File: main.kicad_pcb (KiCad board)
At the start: 2 copper layers, 228.6 x 70.6 mm, 134 parts, among them J1 Conn_02x16_Row_Letter_First, J10 Conn_01x26_Pin, J11 Conn_ARM_JTAG_SWD_10, J2 Conn_01x05, J3 Conn_01x02, J4 Screw_Terminal_01x02, J5 Screw_Terminal_01x10, J6 Screw_Terminal_01x10, J7 Screw_Terminal_01x02, J8 Screw_Terminal_01x10, J9 Screw_Terminal_01x10, U10 TLP3558A, U11 TLP3558A, U12 TLP3558A, U13 TLP3558A, U14 TLP3558A, U15 TLP3558A, U16 TLP3558A, U17 TLP3558A, U18 TLP3558A, U19 TLP3558A, U2 NCP1117-3.3_TO252, U20 TLP3558A, U21 TLP3558A, U22 TLP3558A, U23 TLP3558A, U24 TLP3558A, U25 TLP3558A, U26 TLP3558A, U27 TLP3558A, U28 TLP3558A, U29 TLP3558A, U3 STM32G070KBT6, U30 TLP3558A, U31 TLP3558A, U32 TLP3558A, U33 TLP3558A, U34 TLP3558A, U35 TLP3558A, U36 TLP3558A, U37 TLP3558A, U38 TLP3558A, U39 TLP3558A, U4 TLP3558A, U40 TLP3558A, U41 TLP3558A, U42 TLP3558A, U43 TLP3558A, U44 TLP3558A, U45 TLP3558A, U46 TLP3558A, U47 TLP3558A, U5 TLP3558A, U6 TLP3558A, U7 TLP3558A, U8 TLP3558A, U9 TLP3558A

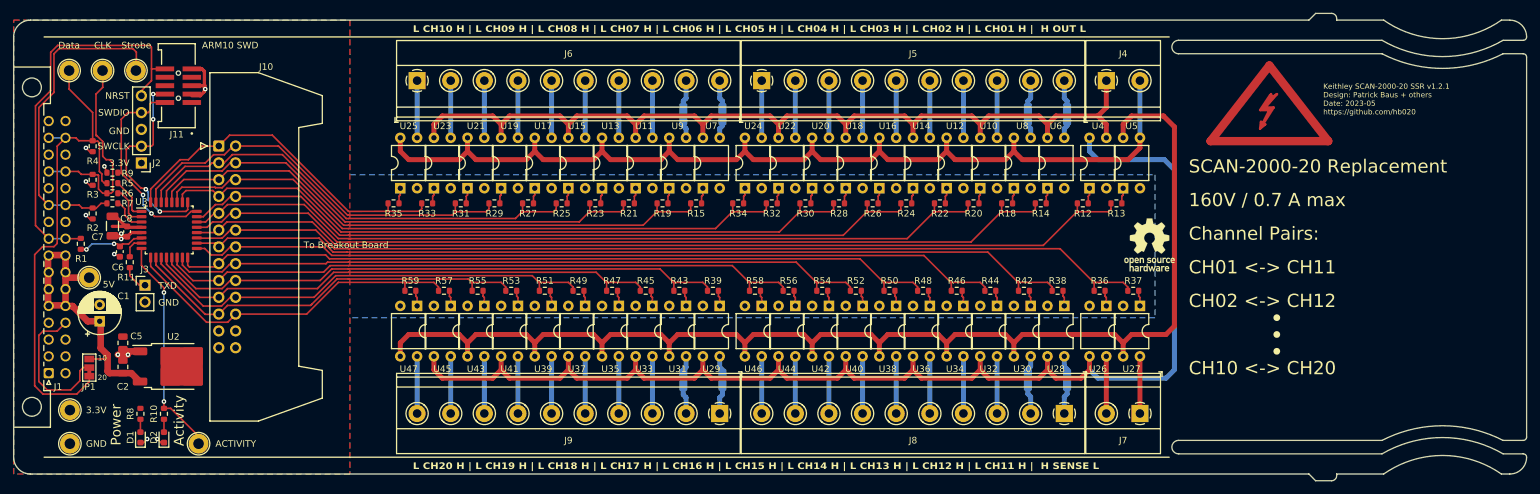
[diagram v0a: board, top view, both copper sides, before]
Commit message: Version 1.6
Created a high-voltage rated scan board.

Control is done completely in logic to avoid programming an MCU
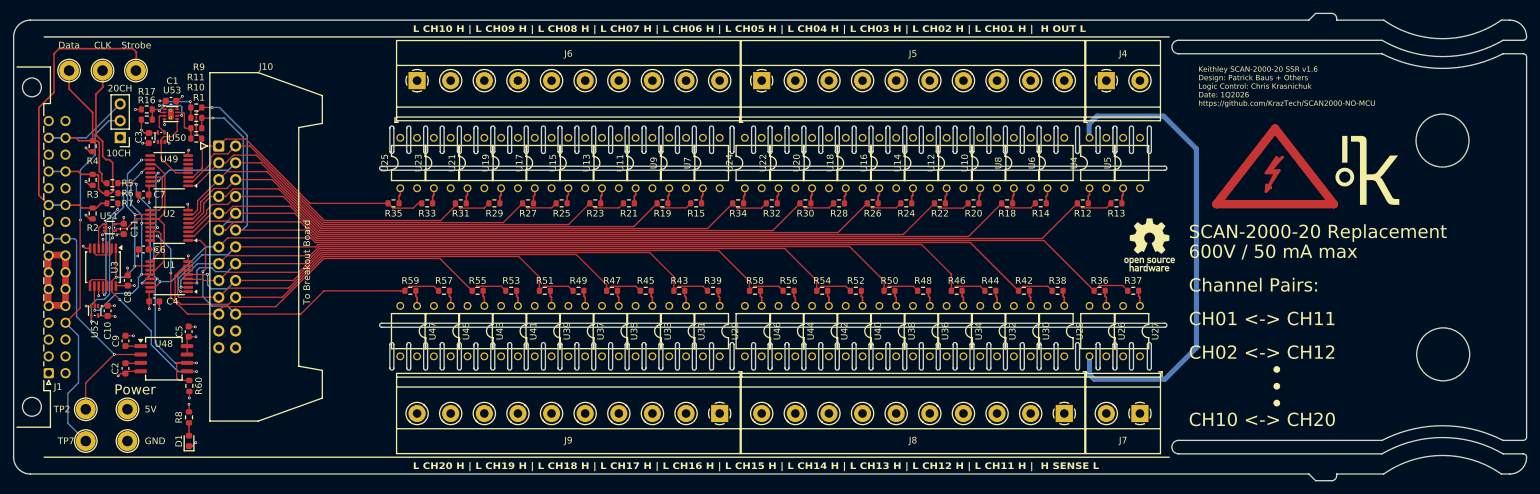
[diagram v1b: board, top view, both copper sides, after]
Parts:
- removed D2: Green, LED_SMD:LED_0603_1608Metric
- removed J11: Conn_ARM_JTAG_SWD_10, Custom_footprints_project:SAMTEC_SHF-105-01-L-D-SM-K-TR
- removed J3: Conn_01x02, Connector_PinHeader_2.54mm:PinHeader_1x02_P2.54mm_Vertical
- removed JP1: SolderJumper_3_Bridged12, Jumper:SolderJumper-3_P1.3mm_Bridged12_Pad1.0x1.5mm_NumberLabels
- removed R40, R41: 2m, Resistor_SMD:R_2512_6332Metric
- added C10: 100n, Capacitor_SMD:C_0603_1608Metric, F.Cu at (39.6, 92.2)
- added C11: 100n, Capacitor_SMD:C_0603_1608Metric, F.Cu at (42.0, 79.8)
- added C3: 100n, Capacitor_SMD:C_0603_1608Metric, F.Cu at (45.8, 66.1)
- added C4: 100n, Capacitor_SMD:C_0603_1608Metric, F.Cu at (46.6, 90.8)
- added C9: 100n, Capacitor_SMD:C_0603_1608Metric, F.Cu at (42.3, 96.7)
- added R60: 1k, Resistor_SMD:R_0603_1608Metric, F.Cu at (52.0, 103.5)
- added U1: SN74ACT595, Package_SO:TSSOP-16_4.4x5mm_P0.65mm, F.Cu at (48.9, 87.0)
- added U48: TL7705AxPS, Package_SO:SOIC-8_5.3x6.2mm_P1.27mm, F.Cu at (48.1, 99.4)
- added U49: SN74ACT595, Package_SO:TSSOP-16_4.4x5mm_P0.65mm, F.Cu at (48.9, 71.0)
- added U50: 74AHC1G04, Package_TO_SOT_SMD:SOT-553, F.Cu at (47.7, 65.9)
- added U51: 74AHC1G08, Package_TO_SOT_SMD:SOT-553, F.Cu at (39.9, 79.6)
- added U52: 74AHC1G04, Package_TO_SOT_SMD:SOT-553, F.Cu at (37.6, 92.2)
- added U53: TLV7012DSGR, Package_SON:Texas_DSG0008A_WSON-8-1EP_2x2mm_P0.5mm_EP0.9x1.6mm_ThermalVias, F.Cu at (49.1, 62.5)
- C1: value 10u -> 100n; footprint Capacitor_THT:CP_Radial_D6.3mm_P2.50mm -> Capacitor_SMD:C_0603_1608Metric
- C2: value 10u -> 100uF; footprint Capacitor_SMD:C_0805_2012Metric -> Capacitor_SMD:C_0603_1608Metric
- C5: value 10u -> 100n; footprint Capacitor_SMD:C_0805_2012Metric -> Capacitor_SMD:C_0603_1608Metric
- C7: value 4.7u -> 100n; footprint Capacitor_SMD:C_1206_3216Metric -> Capacitor_SMD:C_0603_1608Metric
- J2: value Conn_01x05 -> Conn_01x03; footprint Connector_PinHeader_2.54mm:PinHeader_1x05_P2.54mm_Vertical -> Connector_PinHeader_2.54mm:PinHeader_1x03_P2.54mm_Vertical
- R1, R10, R11: value 330R -> 0
- R12, R13, R14, R15, R18, R19, R20, R21, R22, R23, R24, R25, R26, R27, R28, R29, R30, R31, R32, R33, R34, R35, R36, R37, R38, R39, R42, R43, R44, R45, R46, R47, R48, R49, R50, R51, R52, R53, R54, R55, R56, R57, R58, R59: value 330R -> 430R
- R16, R17: value 2m -> 10k; footprint Resistor_SMD:R_2512_6332Metric -> Resistor_SMD:R_0603_1608Metric; moved to F.Cu
- R9: value 10k -> 0
- U10, U11, U12, U13, U14, U15, U16, U17, U18, U19, U20, U21, U22, U23, U24, U25, U26, U27, U28, U29, U30, U31, U32, U33, U34, U35, U36, U37, U38, U39, U4, U40, U41, U42, U43, U44, U45, U46, U47, U5, U6, U7, U8, U9: value TLP3558A -> AQY216EH; footprint Package_DIP:DIP-4_W7.62mm -> Package_DIP:DIP-4_W7.62mm_Least
- U2: value NCP1117-3.3_TO252 -> SN74ACT595; footprint Package_TO_SOT_SMD:TO-252-2 -> Package_SO:TSSOP-16_4.4x5mm_P0.65mm
- U3: value STM32G070KBT6 -> 74HC74; footprint Package_QFP:LQFP-32_7x7mm_P0.8mm -> Package_SO:TSSOP-14_4.4x5mm_P0.65mm
- moved R16 136.1 mm to (45.5, 63.3)
- moved R17 84.0 mm to (45.5, 61.8), turned to 180 degrees
- moved R10 43.4 mm to (53.0, 64.6), turned to 0 degrees
- moved C1 35.0 mm to (49.2, 60.5), turned to 180 degrees
- moved R11 24.0 mm to (53.0, 63.0), turned to 0 degrees
- moved R1 23.6 mm to (53.0, 66.2), turned to 0 degrees
- moved U2 21.3 mm to (48.9, 79.3), turned to 180 degrees
- moved TP1 20.7 mm to (42.6, 107.1)
- moved TP7 17.0 mm to (36.3, 111.9)
- moved R9 16.1 mm to (53.0, 61.5), turned to 0 degrees
- moved U3 11.5 mm to (38.9, 85.6), turned to -90 degrees
- moved C5 10.1 mm to (51.9, 95.3), turned to 90 degrees
- moved SYM1 9.56 mm to (216.0, 72.3)
- moved TP3 8.71 mm to (42.6, 111.9)
- moved C8 7.39 mm to (42.6, 87.6), turned to 90 degrees
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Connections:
- C2 pad 1: +5V -> Net-(U48-CT)
- C5 pad 1: +3.3V -> +5V
- C6 pad 1: Net-(U3-NRST) -> +5V
- C7 pad 1: +3.3V -> +5V
- C8 pad 1: +3.3V -> +5V
- J10 pad 1: /Microcontroller/CH10 -> /Control Logic/CH10
- J10 pad 10: /Microcontroller/CH1 -> /Control Logic/CH1
- J10 pad 11: /Microcontroller/Bus2_input_enable -> /Control Logic/BUS-EN
- J10 pad 12: /Microcontroller/Bus2_sense_enable -> /Control Logic/SENSE-EN
- J10 pad 13: /Microcontroller/CH11 -> /Control Logic/CH11
- J10 pad 14: /Microcontroller/CH12 -> /Control Logic/CH12
- J10 pad 15: /Microcontroller/CH13 -> /Control Logic/CH13
- J10 pad 16: /Microcontroller/CH14 -> /Control Logic/CH14
- J10 pad 17: /Microcontroller/CH15 -> /Control Logic/CH15
- J10 pad 18: /Microcontroller/CH16 -> /Control Logic/CH16
- J10 pad 19: /Microcontroller/CH17 -> /Control Logic/CH17
- J10 pad 2: /Microcontroller/CH9 -> /Control Logic/CH9
- J10 pad 20: /Microcontroller/CH18 -> /Control Logic/CH18
- J10 pad 21: /Microcontroller/CH19 -> /Control Logic/CH19
- J10 pad 22: /Microcontroller/CH20 -> /Control Logic/CH20
- J10 pad 23: +3.3V -> +5V
- J10 pad 24: +3.3V -> +5V
- J10 pad 3: /Microcontroller/CH8 -> /Control Logic/CH8
- J10 pad 4: /Microcontroller/CH7 -> /Control Logic/CH7
- J10 pad 5: /Microcontroller/CH6 -> /Control Logic/CH6
- J10 pad 6: /Microcontroller/CH5 -> /Control Logic/CH5
- J10 pad 7: /Microcontroller/CH4 -> /Control Logic/CH4
- J10 pad 8: /Microcontroller/CH3 -> /Control Logic/CH3
- J10 pad 9: /Microcontroller/CH2 -> /Control Logic/CH2
- J2 pad 1: +3.3V -> +5V
- J2 pad 2: /Microcontroller/SWCLK -> /ID
- J2 pad 3: GND -> /DATA
- R1 pad 1: Net-(U3-NRST) -> Net-(R1-Pad1)
- R1 pad 2: /~{NRST} -> /Control Logic/SENSE-EN
- R10 pad 1: /Microcontroller/LED -> Net-(R1-Pad1)
- R10 pad 2: Net-(D2-A) -> /Control Logic/BUS-EN
- R11 pad 1: Net-(J3-Pin_1) -> Net-(R11-Pad1)
- R11 pad 2: /Microcontroller/TX -> /Control Logic/BUS-EN
- R12 pad 2: /Microcontroller/Bus2_input_enable -> /Control Logic/BUS-EN
- R13 pad 2: /Microcontroller/Bus2_input_enable -> /Control Logic/BUS-EN
- R14 pad 2: /Microcontroller/CH1 -> /Control Logic/CH1
- R15 pad 2: /Microcontroller/CH6 -> /Control Logic/CH6
- R16 pad 1: Net-(J5-Pin_9) -> +5V
- R16 pad 2: Net-(J5-Pin_10) -> Net-(U53A--)
- R17 pad 1: Net-(J6-Pin_9) -> Net-(U53A--)
- R17 pad 2: Net-(J6-Pin_10) -> GND
- R18 pad 2: /Microcontroller/CH1 -> /Control Logic/CH1
- R19 pad 2: /Microcontroller/CH6 -> /Control Logic/CH6
- R20 pad 2: /Microcontroller/CH2 -> /Control Logic/CH2
- R21 pad 2: /Microcontroller/CH7 -> /Control Logic/CH7
- R22 pad 2: /Microcontroller/CH2 -> /Control Logic/CH2
- R23 pad 2: /Microcontroller/CH7 -> /Control Logic/CH7
- R24 pad 2: /Microcontroller/CH3 -> /Control Logic/CH3
- R25 pad 2: /Microcontroller/CH8 -> /Control Logic/CH8
- R26 pad 2: /Microcontroller/CH3 -> /Control Logic/CH3
- R27 pad 2: /Microcontroller/CH8 -> /Control Logic/CH8
- R28 pad 2: /Microcontroller/CH4 -> /Control Logic/CH4
- R29 pad 2: /Microcontroller/CH9 -> /Control Logic/CH9
- R30 pad 2: /Microcontroller/CH4 -> /Control Logic/CH4
- R31 pad 2: /Microcontroller/CH9 -> /Control Logic/CH9
- R32 pad 2: /Microcontroller/CH5 -> /Control Logic/CH5
- R33 pad 2: /Microcontroller/CH10 -> /Control Logic/CH10
- R34 pad 2: /Microcontroller/CH5 -> /Control Logic/CH5
- R35 pad 2: /Microcontroller/CH10 -> /Control Logic/CH10
- R36 pad 2: /Microcontroller/Bus2_sense_enable -> /Control Logic/SENSE-EN
- R37 pad 2: /Microcontroller/Bus2_sense_enable -> /Control Logic/SENSE-EN
- R38 pad 2: /Microcontroller/CH11 -> /Control Logic/CH11
- R39 pad 2: /Microcontroller/CH16 -> /Control Logic/CH16
- R42 pad 2: /Microcontroller/CH11 -> /Control Logic/CH11
- R43 pad 2: /Microcontroller/CH16 -> /Control Logic/CH16
- R44 pad 2: /Microcontroller/CH12 -> /Control Logic/CH12
- R45 pad 2: /Microcontroller/CH17 -> /Control Logic/CH17
- R46 pad 2: /Microcontroller/CH12 -> /Control Logic/CH12
- R47 pad 2: /Microcontroller/CH17 -> /Control Logic/CH17
- R48 pad 2: /Microcontroller/CH13 -> /Control Logic/CH13
- R49 pad 2: /Microcontroller/CH18 -> /Control Logic/CH18
- R5 pad 1: /Microcontroller/DATA -> /Control Logic/DATA
- R50 pad 2: /Microcontroller/CH13 -> /Control Logic/CH13
- R51 pad 2: /Microcontroller/CH18 -> /Control Logic/CH18
- R52 pad 2: /Microcontroller/CH14 -> /Control Logic/CH14
- R53 pad 2: /Microcontroller/CH19 -> /Control Logic/CH19
- R54 pad 2: /Microcontroller/CH14 -> /Control Logic/CH14
- R55 pad 2: /Microcontroller/CH19 -> /Control Logic/CH19
- R56 pad 2: /Microcontroller/CH15 -> /Control Logic/CH15
- R57 pad 2: /Microcontroller/CH20 -> /Control Logic/CH20
- R58 pad 2: /Microcontroller/CH15 -> /Control Logic/CH15
- R59 pad 2: /Microcontroller/CH20 -> /Control Logic/CH20
- R6 pad 1: /Microcontroller/CLK -> /Control Logic/CLK
- R7 pad 1: /Microcontroller/STROBE -> /Control Logic/STROBE
- R8 pad 1: +3.3V -> +5V
- R9 pad 1: /Microcontroller/SWDIO -> Net-(R11-Pad1)
- R9 pad 2: GND -> /Control Logic/SENSE-EN
- TP2 pad 1: +3.3V -> /~{NRST}
- TP7 pad 1: /Microcontroller/LED -> /ID
- U2 pad 1: GND -> /Control Logic/CH20
- U2 pad 2: +3.3V -> /Control Logic/CH1
- U2 pad 3: +5V -> /Control Logic/CH2
- U3 pad 1: /Microcontroller/DATA -> /Control Logic/POR-CLR
- U3 pad 10: /Microcontroller/CH19 -> +5V
- U3 pad 11: /Microcontroller/CH18 -> /Control Logic/STROBE
- U3 pad 12: /Microcontroller/CH17 -> Net-(U3B-D)
- U3 pad 13: /Microcontroller/CH16 -> /Control Logic/POR-CLR
- U3 pad 14: /Microcontroller/CH15 -> +5V
- U3 pad 2: /Microcontroller/CLK -> Net-(U3A-D)
- U3 pad 3: /Microcontroller/STROBE -> /Control Logic/CLK
- U3 pad 4: +3.3V -> +5V
- U3 pad 5: GND -> /Control Logic/CLK-DIV-2
- U3 pad 6: Net-(U3-NRST) -> Net-(U3A-D)
- U3 pad 7: /Microcontroller/TX -> GND
- U3 pad 8: /Microcontroller/LED -> Net-(U3B-D)
- U3 pad 9: /Microcontroller/CH20 -> /Control Logic/STROBE-DIV-2
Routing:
- net /Control Logic/SENSE-EN: track 0.00 -> 168.9 mm, vias 0 -> 1
- net /Control Logic/BUS-EN: track 0.00 -> 165.0 mm, vias 0 -> 1
- net /Microcontroller/Bus2_sense_enable: track 146.7 -> 0.00 mm
- net /Microcontroller/Bus2_input_enable: track 144.1 -> 0.00 mm
- net /Control Logic/CH11: track 0.00 -> 143.4 mm, vias 0 -> 1
- net /Microcontroller/CH11: track 134.7 -> 0.00 mm
- net /Microcontroller/CH1: track 133.8 -> 0.00 mm
- net /Control Logic/CH1: track 0.00 -> 133.5 mm
- net /Control Logic/CH12: track 0.00 -> 132.2 mm, vias 0 -> 1
- net /Microcontroller/CH12: track 124.5 -> 0.00 mm
- net /Control Logic/CH2: track 0.00 -> 123.8 mm
- net /Microcontroller/CH2: track 123.4 -> 0.00 mm
- net /Control Logic/CH13: track 0.00 -> 119.8 mm, vias 0 -> 1
- net /Microcontroller/CH13: track 115.5 -> 0.00 mm
- net /Control Logic/CH3: track 0.00 -> 114.6 mm
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- added copper zone on In2.Cu, net +5V
- added copper zone on In1.Cu, net GND
- removed copper zone on F.Cu, net +3.3V
- removed copper zone on B.Cu, net GND
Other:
- outline, holes or cut-outs redrawn
- copper layers 2 -> 4
- board text added: "10CH"
- board text added: "20CH"
- board text added: "600V / 50 mA max"
- board text added: "Keithley SCAN-2000-20 SSR v1.6 Design: Patrick Baus + Others Logic Control: Chris Krasnichuk Date: 1Q2026 https://github.com/KrazTech/SCAN2000-NO-MCU"
- board text removed: "10"
- board text removed: "160V / 0.7 A max"
- board text removed: "20"
- board text removed: "3.3V"
- board text removed: "ACTIVITY"
- board text removed: "ARM10 SWD"
- board text removed: "Activity"
- board text removed: "Keithley SCAN-2000-20 SSR v1.2.1 Design: Patrick Baus + others Date: 2023-05 https://github.com/hb020"
- board text removed: "NRST"
- board text removed: "SWCLK"
- board text removed: "SWDIO"
- board text removed: "TXD"
